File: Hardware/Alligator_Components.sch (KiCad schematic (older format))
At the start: 114 parts, among them J1 SWD_Header, J2 Eurorack_10_pin_power, J3 Conn_01x08_Female, J4 Conn_01x08_Female, J5 Conn_01x08_Female, J6 Conn_01x08_Female, SW1 SW_SPST, SW2 SW_SPDT_MSM, U1 STM32H743ZITx, U2 IS42S16400J-xC, U3 PCM5100APW, U4 SSI2164, U5 MCP6004, U6 MCP6004, U7 TL074, U8 LM1117-3.3, Y1 8MHz 20pF

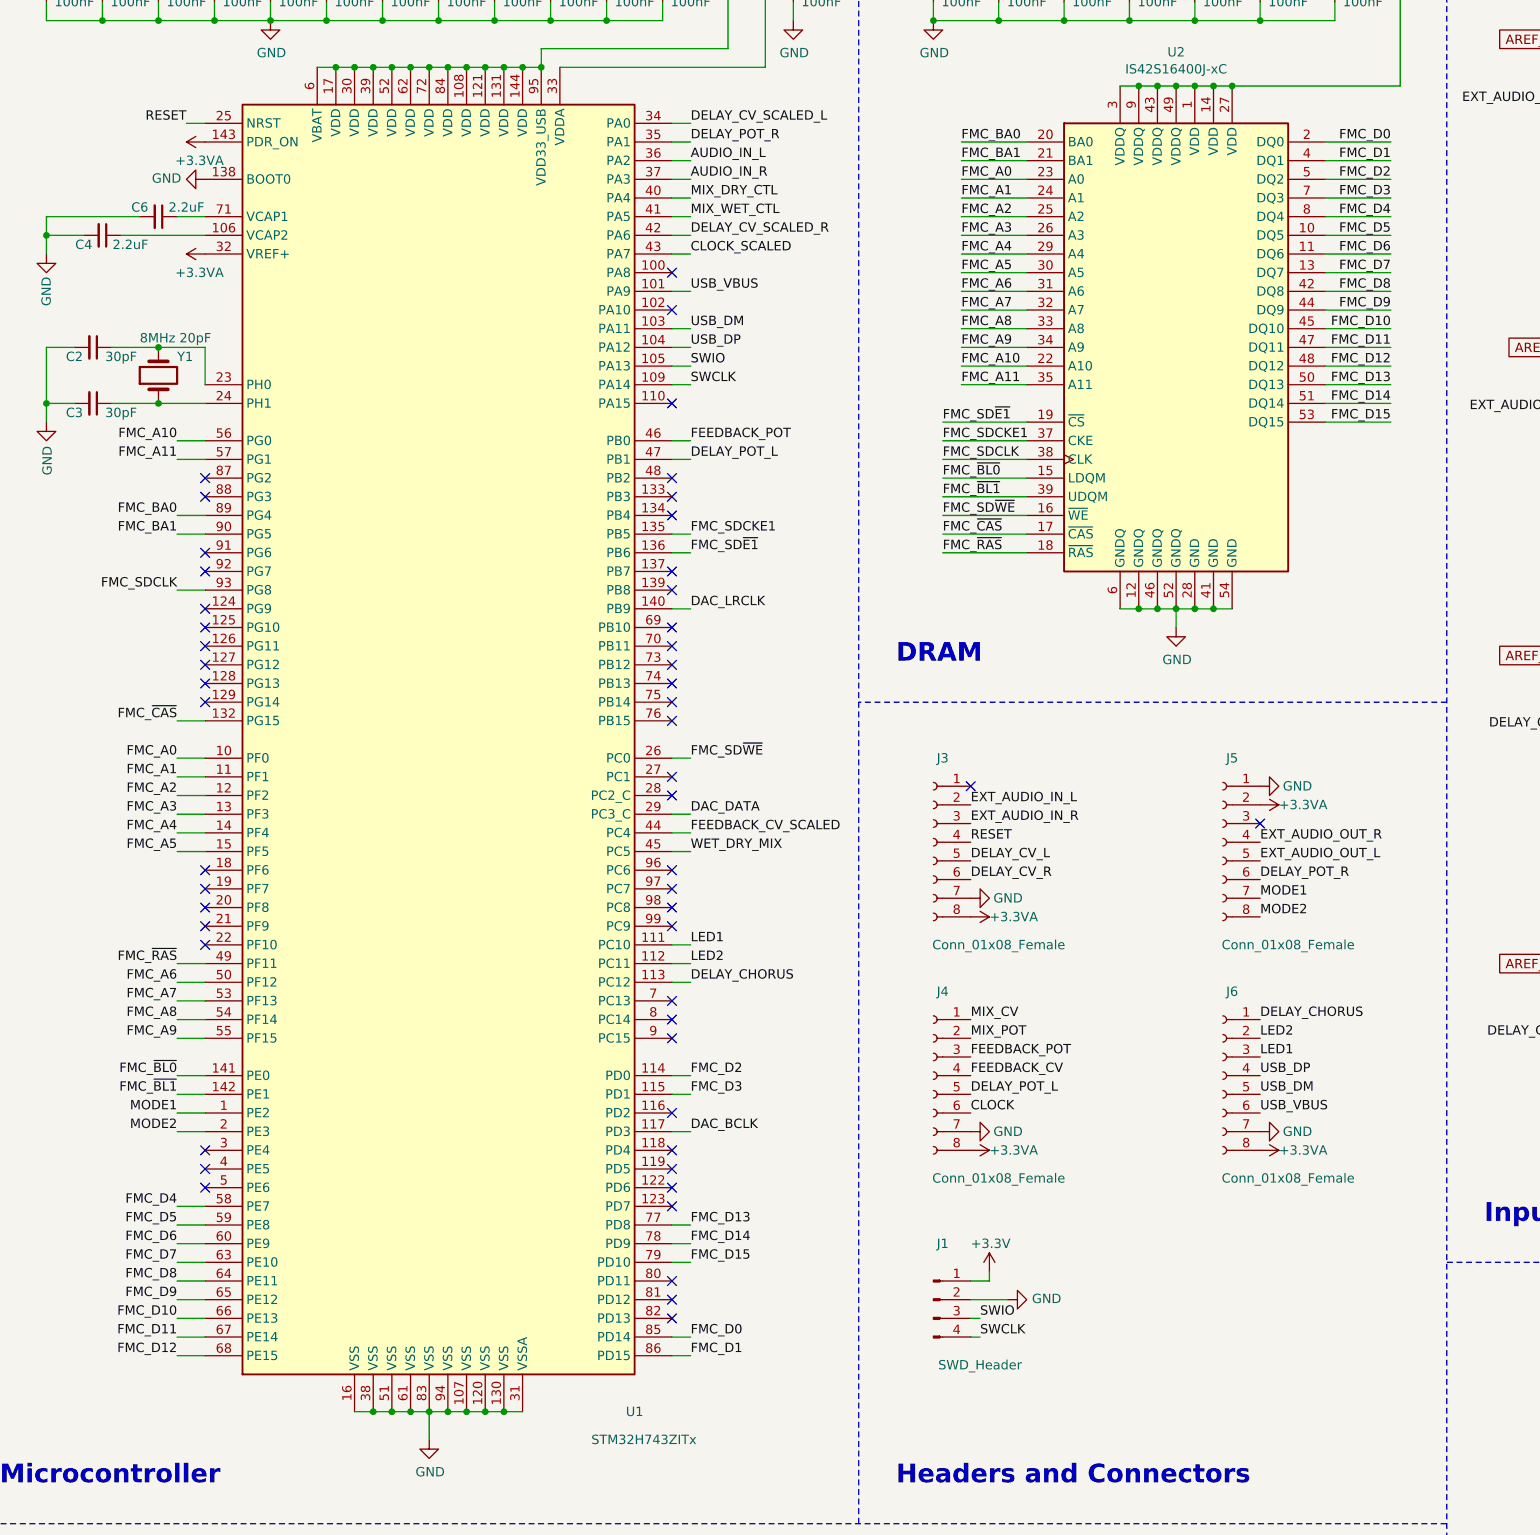
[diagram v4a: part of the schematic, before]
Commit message: Completed PCB routing
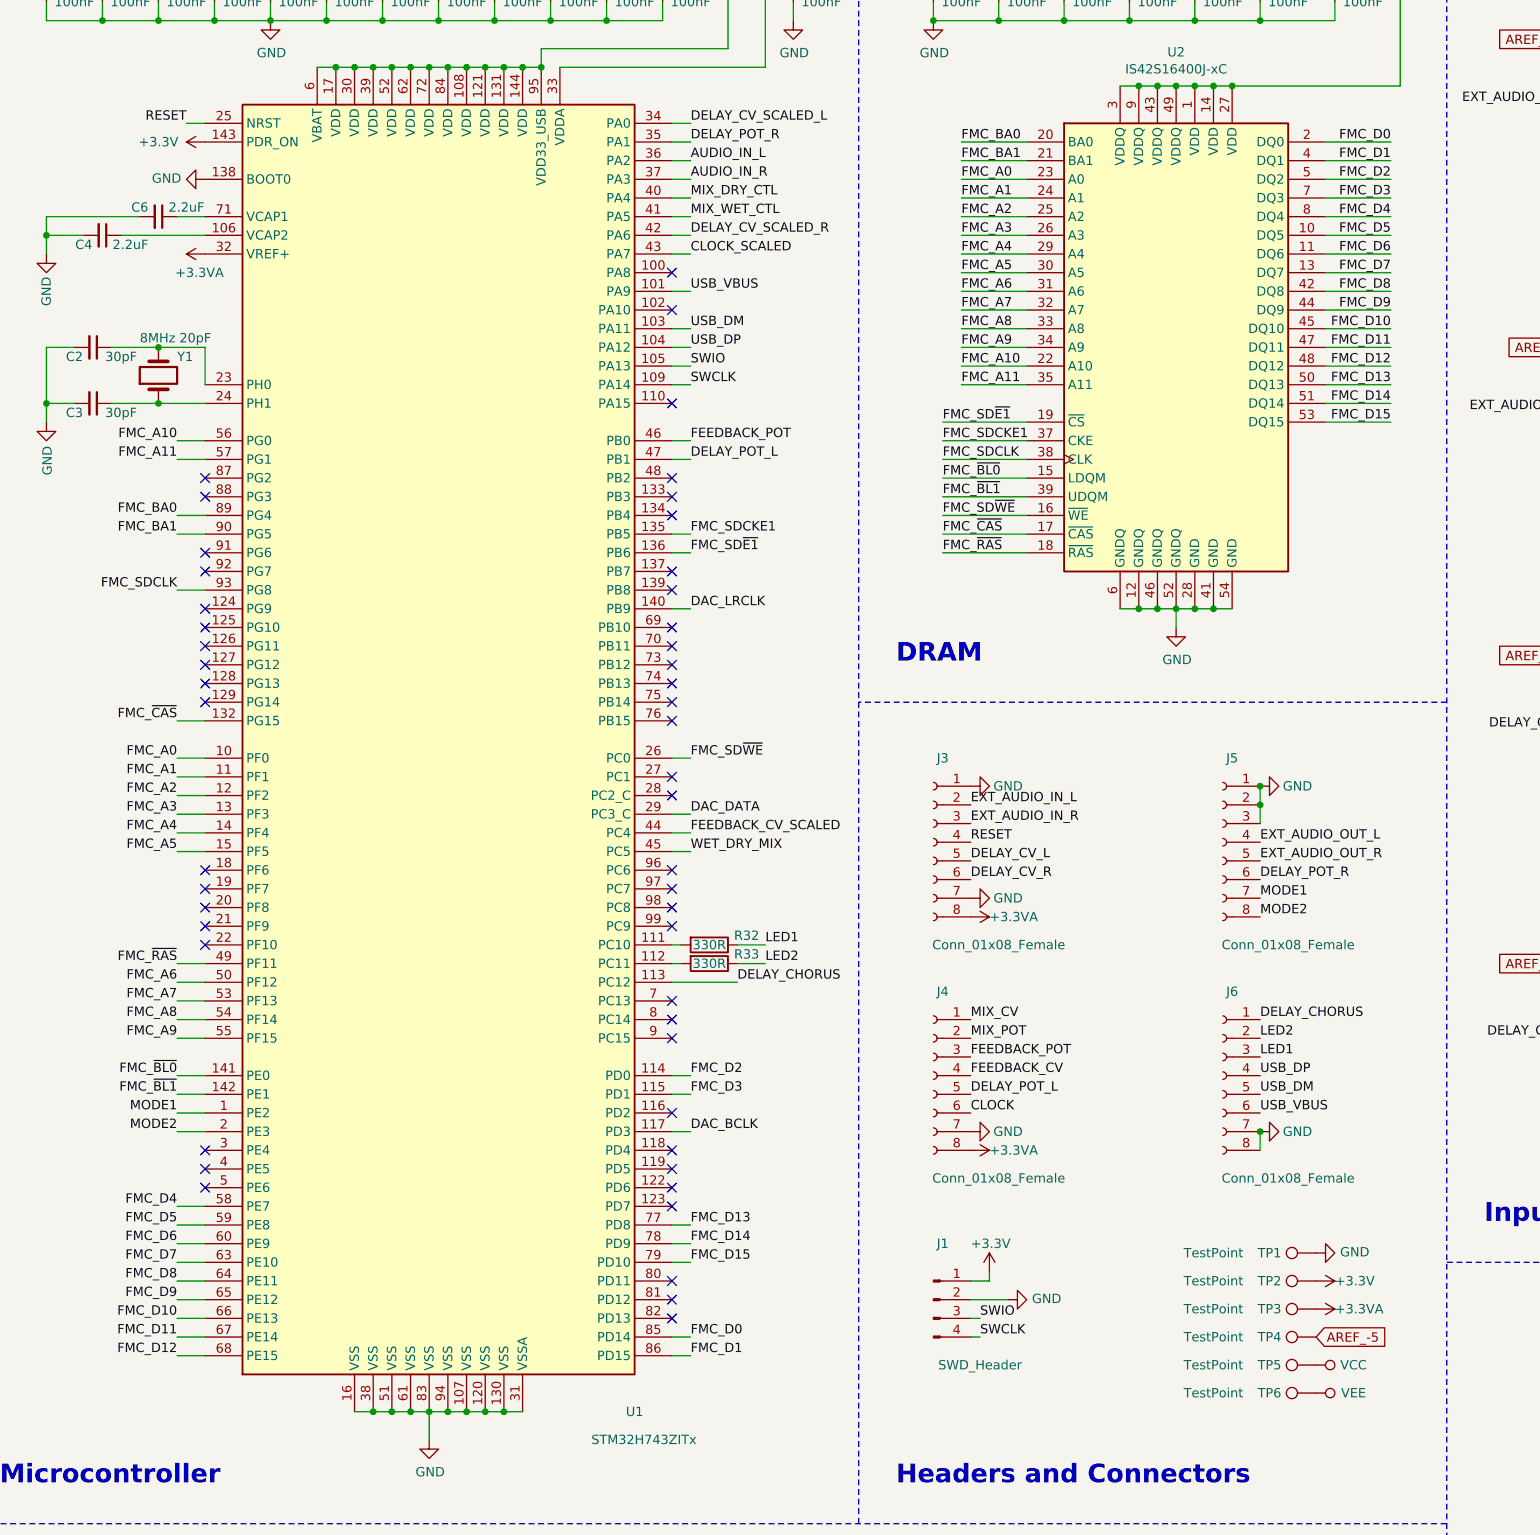
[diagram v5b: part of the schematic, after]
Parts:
- added R32, R33: 330R, Resistors_SMD:R_0603_HandSoldering, symbol Device:R
- added TP1, TP2, TP3, TP4, TP5, TP6: TestPoint, Measurement_Points:Test_Point_Keystone_5005-5009_Compact, symbol Connector:TestPoint
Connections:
- net +3.3VA: now also TP3.1; no longer J5.2 (Pin_2), J6.8 (Pin_8), U1.143 (PDR_ON)
- net +3V3: now also U1.143 (PDR_ON), TP2.1
- net AREF_-5: now also TP4.1
- net EXT_AUDIO_OUT_L: now also J5.4 (Pin_4); no longer J5.5 (Pin_5)
- net EXT_AUDIO_OUT_R: now also J5.5 (Pin_5); no longer J5.4 (Pin_4)
- net GND: now also J3.1 (Pin_1), J5.2 (Pin_2), J5.3 (Pin_3), J6.8 (Pin_8), TP1.1
- net LED1: now also R32.1; no longer U1.111 (PC10)
- net LED2: now also R33.1; no longer U1.112 (PC11)
- net VCC: now also TP5.1
- net VEE: now also TP6.1
- new net: R32.2, U1.111 (PC10)
- new net: R33.2, U1.112 (PC11)
- no-connect marks 69 -> 67
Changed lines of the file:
@@
 Wire Wire Line
 	5800 2250 6150 2250
-$Comp
-L power:+3.3VA #PWR0114
-U 1 1 60B4FB5F
-P 1750 2050
-F 0 "#PWR0114" H 1750 1900 50  0001 C CNN
-F 1 "+3.3VA" V 1650 1950 50  0000 L CNN
-F 2 "" H 1750 2050 50  0001 C CNN
-F 3 "" H 1750 2050 50  0001 C CNN
-	1    1750 2050
-	0    -1   -1   0
-$EndComp
 Wire Wire Line
 	3450 1650 3550 1650
@@
 Text Label 5850 5600 0    50   ~ 0
 EXT_AUDIO_IN_L
+Text Label 7400 5900 0    50   ~ 0
+EXT_AUDIO_OUT_R
 Text Label 7400 5800 0    50   ~ 0
-EXT_AUDIO_OUT_R
-Text Label 7400 5900 0    50   ~ 0
 EXT_AUDIO_OUT_L
 Text Label 16450 6800 0    50   ~ 0
@@
 F 3 "~" H 5650 7050 50  0001 C CNN
 	1    5650 7050
-	-1   0    0    -1
-$EndComp
-$Comp
-L Connector:Conn_01x08_Female J6
-U 1 1 60832E97
-P 7200 7050
-F 0 "J6" H 7150 7500 50  0000 C CNN
-F 1 "Conn_01x08_Female" H 6850 6500 50  0000 C CNN
-F 2 "Socket_Strips:Socket_Strip_Straight_1x08_Pitch2.54mm" H 7200 7050 50  0001 C CNN
-F 3 "~" H 7200 7050 50  0001 C CNN
-	1    7200 7050
 	-1   0    0    -1
 $EndComp
@@
 $EndComp
 $Comp
-L power:+3.3VA #PWR013
-U 1 1 6196317E
-P 7400 7450
-F 0 "#PWR013" H 7400 7300 50  0001 C CNN
-F 1 "+3.3VA" V 7400 7550 50  0000 L CNN
-F 2 "" H 7400 7450 50  0001 C CNN
-F 3 "" H 7400 7450 50  0001 C CNN
-	1    7400 7450
-	0    1    1    0
-$EndComp
-$Comp
 L power:+3.3VA #PWR09
 U 1 1 619635CF
@@
 Wire Wire Line
 	1750 7350 1600 7350
-Text Label 4350 6350 0    50   ~ 0
+Text Label 4750 6350 0    50   ~ 0
 LED1
-Text Label 4350 6450 0    50   ~ 0
+Text Label 4750 6450 0    50   ~ 0
 LED2
 Wire Wire Line
-	4250 6350 4350 6350
-Wire Wire Line
-	4250 6450 4350 6450
+	4250 6350 4300 6350
+Wire Wire Line
+	4250 6450 4300 6450
 Text Label 4350 3650 0    50   ~ 0
 FEEDBACK_POT
@@
 	0    -1   -1   0
 $EndComp
-$Comp
-L power:+3.3VA #PWR0124
-U 1 1 60A82817
-P 7400 5600
-F 0 "#PWR0124" H 7400 5450 50  0001 C CNN
-F 1 "+3.3VA" V 7400 5700 50  0000 L CNN
-F 2 "" H 7400 5600 50  0001 C CNN
-F 3 "" H 7400 5600 50  0001 C CNN
-	1    7400 5600
-	0    1    1    0
-$EndComp
-Text Label 4350 6550 0    50   ~ 0
+Text Label 4600 6550 0    50   ~ 0
 DELAY_CHORUS
 Wire Wire Line
 	2450 1650 2550 1650
 Wire Wire Line
-	4250 6550 4350 6550
+	4250 6550 4600 6550
 NoConn ~ 4250 6050
 NoConn ~ 4250 6150
@@
 	2350 1650 2450 1650
 Connection ~ 2450 1650
-NoConn ~ 7400 5700
-NoConn ~ 5850 5500
+$Comp
+L Connector:Conn_01x08_Female J6
+U 1 1 60832E97
+P 7200 7050
+F 0 "J6" H 7150 7500 50  0000 C CNN
+F 1 "Conn_01x08_Female" H 6850 6500 50  0000 C CNN
+F 2 "Socket_Strips:Socket_Strip_Straight_1x08_Pitch2.54mm" H 7200 7050 50  0001 C CNN
+F 3 "~" H 7200 7050 50  0001 C CNN
+	1    7200 7050
+	-1   0    0    -1
+$EndComp
+Wire Wire Line
+	7400 7450 7400 7350
+Connection ~ 7400 7350
+$Comp
+L power:+3.3V #PWR0114
+U 1 1 5F992632
+P 1750 2050
+F 0 "#PWR0114" H 1750 1900 50  0001 C CNN
+F 1 "+3.3V" V 1750 2300 50  0000 C CNN
+F 2 "" H 1750 2050 50  0001 C CNN
+F 3 "" H 1750 2050 50  0001 C CNN
+	1    1750 2050
+	0    -1   -1   0
+$EndComp
+$Comp
+L power:GND #PWR0124
+U 1 1 5FA6DF94
+P 5850 5500
+F 0 "#PWR0124" H 5850 5250 50  0001 C CNN
+F 1 "GND" V 5850 5300 50  0000 C CNN
+F 2 "" H 5850 5500 50  0001 C CNN
+F 3 "" H 5850 5500 50  0001 C CNN
+	1    5850 5500
+	0    -1   -1   0
+$EndComp
+Wire Wire Line
+	7400 5700 7400 5600
+Connection ~ 7400 5500
+Connection ~ 7400 5600
+Wire Wire Line
+	7400 5600 7400 5500
+$Comp
+L Connector:TestPoint TP1
+U 1 1 5FBC76F3
+P 7700 8000
+F 0 "TP1" V 7700 8250 50  0000 C CNN
+F 1 "TestPoint" V 7700 8550 50  0000 C CNN
+F 2 "Measurement_Points:Test_Point_Keystone_5005-5009_Compact" H 7900 8000 50  0001 C CNN
+F 3 "~" H 7900 8000 50  0001 C CNN
+	1    7700 8000
+	0    -1   -1   0
+$EndComp
+$Comp
+L power:GND #PWR010
+U 1 1 5FBC7DF8
+P 7700 8000
+F 0 "#PWR010" H 7700 7750 50  0001 C CNN
+F 1 "GND" V 7705 7872 50  0000 R CNN
+F 2 "" H 7700 8000 50  0001 C CNN
+F 3 "" H 7700 8000 50  0001 C CNN
+	1    7700 8000
+	0    -1   -1   0
+$EndComp
+$Comp
+L Connector:TestPoint TP2
+U 1 1 5FBC80EE
+P 7700 8150
+F 0 "TP2" V 7700 8400 50  0000 C CNN
+F 1 "TestPoint" V 7700 8700 50  0000 C CNN
+F 2 "Measurement_Points:Test_Point_Keystone_5005-5009_Compact" H 7900 8150 50  0001 C CNN
+F 3 "~" H 7900 8150 50  0001 C CNN
+	1    7700 8150
+	0    -1   -1   0
+$EndComp
+$Comp
+L power:+3.3V #PWR011
+U 1 1 5FBC8425
+P 7700 8150
+F 0 "#PWR011" H 7700 8000 50  0001 C CNN
+F 1 "+3.3V" V 7700 8250 50  0000 L CNN
+F 2 "" H 7700 8150 50  0001 C CNN
+F 3 "" H 7700 8150 50  0001 C CNN
+	1    7700 8150
+	0    1    1    0
+$EndComp
+$Comp
+L Connector:TestPoint TP3
+U 1 1 5FBC8AAF
+P 7700 8300
+F 0 "TP3" V 7700 8550 50  0000 C CNN
+F 1 "TestPoint" V 7700 8850 50  0000 C CNN
+F 2 "Measurement_Points:Test_Point_Keystone_5005-5009_Compact" H 7900 8300 50  0001 C CNN
+F 3 "~" H 7900 8300 50  0001 C CNN
+	1    7700 8300
+	0    -1   -1   0
+$EndComp
+$Comp
+L power:+3.3VA #PWR013
+U 1 1 5FBC8BDD
+P 7700 8300
+F 0 "#PWR013" H 7700 8150 50  0001 C CNN
+F 1 "+3.3VA" V 7700 8400 50  0000 L CNN
+F 2 "" H 7700 8300 50  0001 C CNN
+F 3 "" H 7700 8300 50  0001 C CNN
+	1    7700 8300
+	0    1    1    0
+$EndComp
+$Comp
+L Connector:TestPoint TP4
+U 1 1 5FBC8F33
+P 7700 8450
+F 0 "TP4" V 7700 8700 50  0000 C CNN
+F 1 "TestPoint" V 7700 9000 50  0000 C CNN
+F 2 "Measurement_Points:Test_Point_Keystone_5005-5009_Compact" H 7900 8450 50  0001 C CNN
+F 3 "~" H 7900 8450 50  0001 C CNN
+	1    7700 8450
+	0    -1   -1   0
+$EndComp
+Text GLabel 7700 8450 2    50   Input ~ 0
+AREF_-5
+$Comp
+L Connector:TestPoint TP5
+U 1 1 5FBC912F
+P 7700 8600
+F 0 "TP5" V 7700 8850 50  0000 C CNN
+F 1 "TestPoint" V 7700 9150 50  0000 C CNN
+F 2 "Measurement_Points:Test_Point_Keystone_5005-5009_Compact" H 7900 8600 50  0001 C CNN
+F 3 "~" H 7900 8600 50  0001 C CNN
+	1    7700 8600
+	0    -1   -1   0
+$EndComp
+$Comp
+L Connector:TestPoint TP6
+U 1 1 5FBC9283
+P 7700 8750
+F 0 "TP6" V 7700 9000 50  0000 C CNN
+F 1 "TestPoint" V 7700 9300 50  0000 C CNN
+F 2 "Measurement_Points:Test_Point_Keystone_5005-5009_Compact" H 7900 8750 50  0001 C CNN
+F 3 "~" H 7900 8750 50  0001 C CNN
+	1    7700 8750
+	0    -1   -1   0
+$EndComp
+$Comp
+L power:VEE #PWR019
+U 1 1 5FBC93A3
+P 7700 8750
+F 0 "#PWR019" H 7700 8600 50  0001 C CNN
+F 1 "VEE" V 7700 8950 50  0000 C CNN
+F 2 "" H 7700 8750 50  0001 C CNN
+F 3 "" H 7700 8750 50  0001 C CNN
+	1    7700 8750
+	0    1    1    0
+$EndComp
+$Comp
+L power:VCC #PWR018
+U 1 1 5FBC9909
+P 7700 8600
+F 0 "#PWR018" H 7700 8450 50  0001 C CNN
+F 1 "VCC" V 7700 8800 50  0000 C CNN
+F 2 "" H 7700 8600 50  0001 C CNN
+F 3 "" H 7700 8600 50  0001 C CNN
+	1    7700 8600
+	0    1    1    0
+$EndComp
+$Comp
+L Device:R R32
+U 1 1 5FE3B49C
+P 4450 6350
+F 0 "R32" V 4400 6550 50  0000 C CNN
+F 1 "330R" V 4450 6350 50  0000 C CNN
+F 2 "Resistors_SMD:R_0603_HandSoldering" V 4380 6350 50  0001 C CNN
+F 3 "~" H 4450 6350 50  0001 C CNN
+	1    4450 6350
+	0    1    1    0
+$EndComp
+Wire Wire Line
+	4600 6350 4750 6350
+$Comp
+L Device:R R33
+U 1 1 5FEA3045
+P 4450 6450
+F 0 "R33" V 4400 6650 50  0000 C CNN
+F 1 "330R" V 4450 6450 50  0000 C CNN
+F 2 "Resistors_SMD:R_0603_HandSoldering" V 4380 6450 50  0001 C CNN
+F 3 "~" H 4450 6450 50  0001 C CNN
+	1    4450 6450
+	0    1    1    0
+$EndComp
+Wire Wire Line
+	4600 6450 4750 6450
 $EndSCHEMATC
